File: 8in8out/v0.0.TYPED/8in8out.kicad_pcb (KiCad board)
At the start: 2 copper layers, 100.1 x 86.4 mm, 61 parts, among them IC1 ATTINY48-A, J1 RJ45, J2 RJ45, J3 CONN_6, K110 G5T-1-12VDC, K120 G5T-1-12VDC, K130 G5T-1-12VDC, K140 G5T-1-12VDC, K150 G5T-1-12VDC, K160 G5T-1-12VDC, K170 G5T-1-12VDC, K180 G5T-1-12VDC, P1 CONN_5, P100 CONN_2, P101 CONN_2, P102 CONN_2, P103 CONN_2, P105 CONN_2, P106 CONN_2, P110 CONN_2, P120 CONN_2, P130 CONN_2, P140 CONN_2, P150 CONN_2, P160 CONN_2, P170 CONN_2, P180 CONN_2, P2 CONN_5, P3 CONN_10X2, P4 CONN_2, U1 7805, U10 OPTO-TRANSISTOR, U2 ULN2803, U20 OPTO-TRANSISTOR, U30 OPTO-TRANSISTOR, U40 OPTO-TRANSISTOR, U50 OPTO-TRANSISTOR, U60 OPTO-TRANSISTOR, U70 OPTO-TRANSISTOR, U80 OPTO-TRANSISTOR

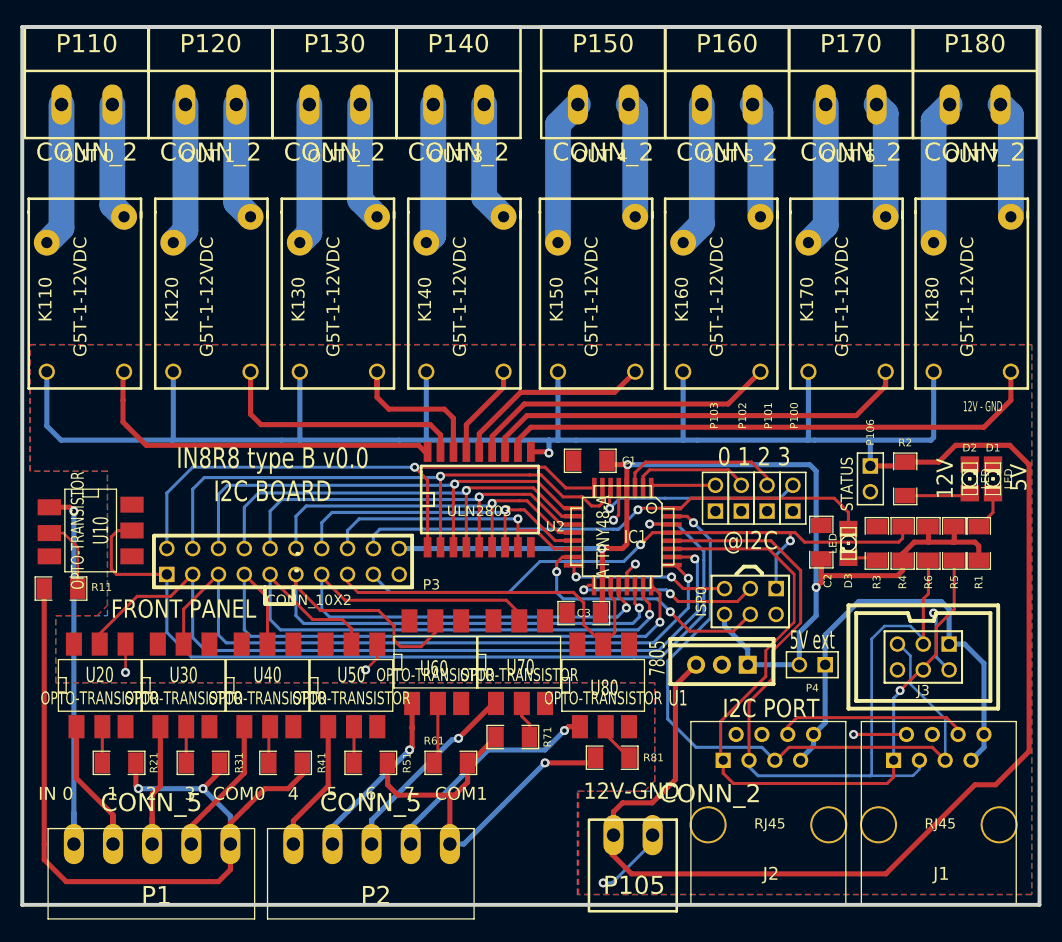
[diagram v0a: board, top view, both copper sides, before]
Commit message: correction connecteur ISP
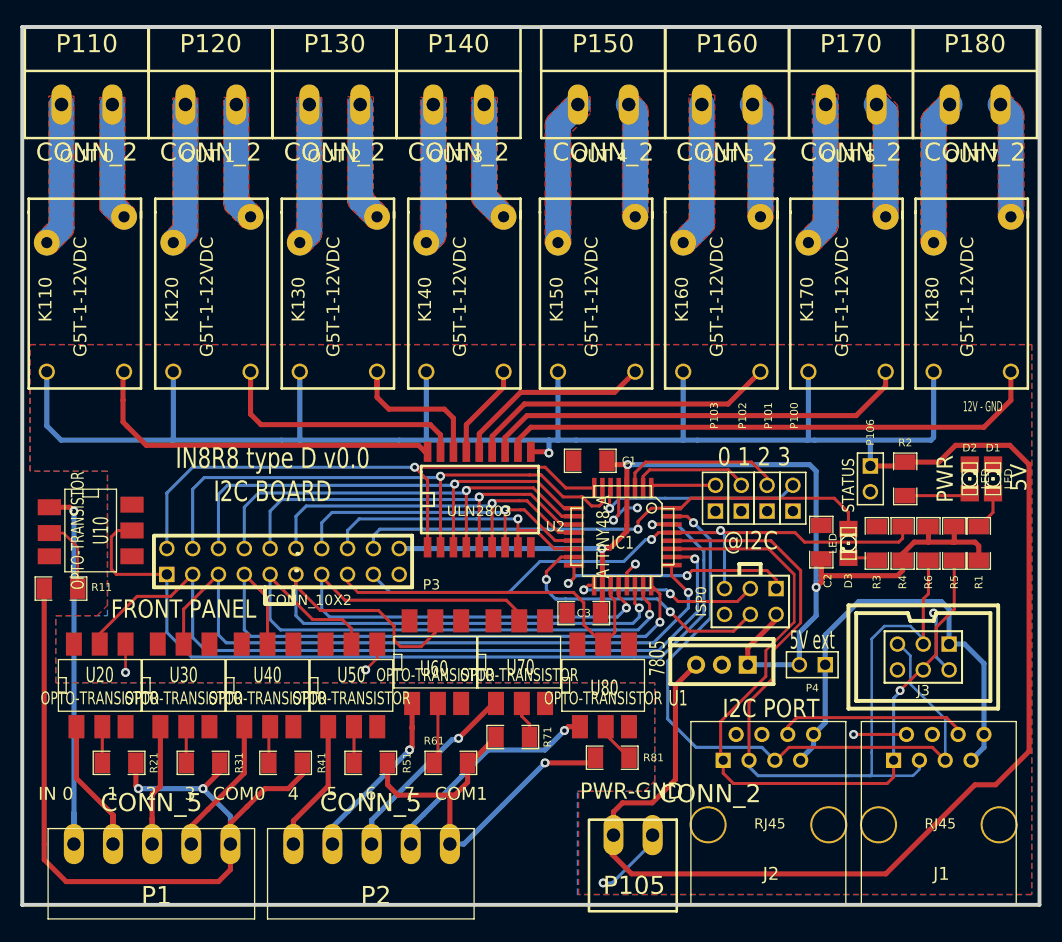
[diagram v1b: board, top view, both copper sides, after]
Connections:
- ISP0 pad 1: RESET -> MISO
- ISP0 pad 2: GND -> +5V
- ISP0 pad 5: MISO -> RESET
- ISP0 pad 6: +5V -> GND
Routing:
- net MISO: track 16.3 -> 24.4 mm
- net GND: track 50.5 -> 53.4 mm, vias 7 -> 8
- net CMD0: track 87.3 -> 89.1 mm
- net MOSI: track 26.2 -> 27.5 mm
- net +5V: track 116.1 -> 115.5 mm
- added copper zone on F.Cu, net /230_110_1
- added copper zone on F.Cu, net /230_110_2
- added copper zone on F.Cu, net /230_120_1
- added copper zone on F.Cu, net /230_120_2
- added copper zone on F.Cu, net /230_130_1
- added copper zone on F.Cu, net /230_130_2
- added copper zone on F.Cu, net /230_140_1
- added copper zone on F.Cu, net /230_140_2
- added copper zone on F.Cu, net /230_150_1
- added copper zone on F.Cu, net /230_150_2
- added copper zone on F.Cu, net /230_160_1
- added copper zone on F.Cu, net /230_160_2
- added copper zone on F.Cu, net /230_170_1
- added copper zone on F.Cu, net /230_170_2
- added copper zone on F.Cu, net /230_180_1
- added copper zone on F.Cu, net /230_180_2
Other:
- board text added: "IN8R8 type D v0.0 I2C BOARD"
- board text added: "PWR"
- board text added: "PWR-GND"
- board text removed: "12V"
- board text removed: "12V-GND"
- board text removed: "IN8R8 type B v0.0 I2C BOARD"

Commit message: reprise connecteur correction mask back connecteur 230v serigraphie complete double piste relais cot? puissance verification routage generation gerber bon pour fab ?
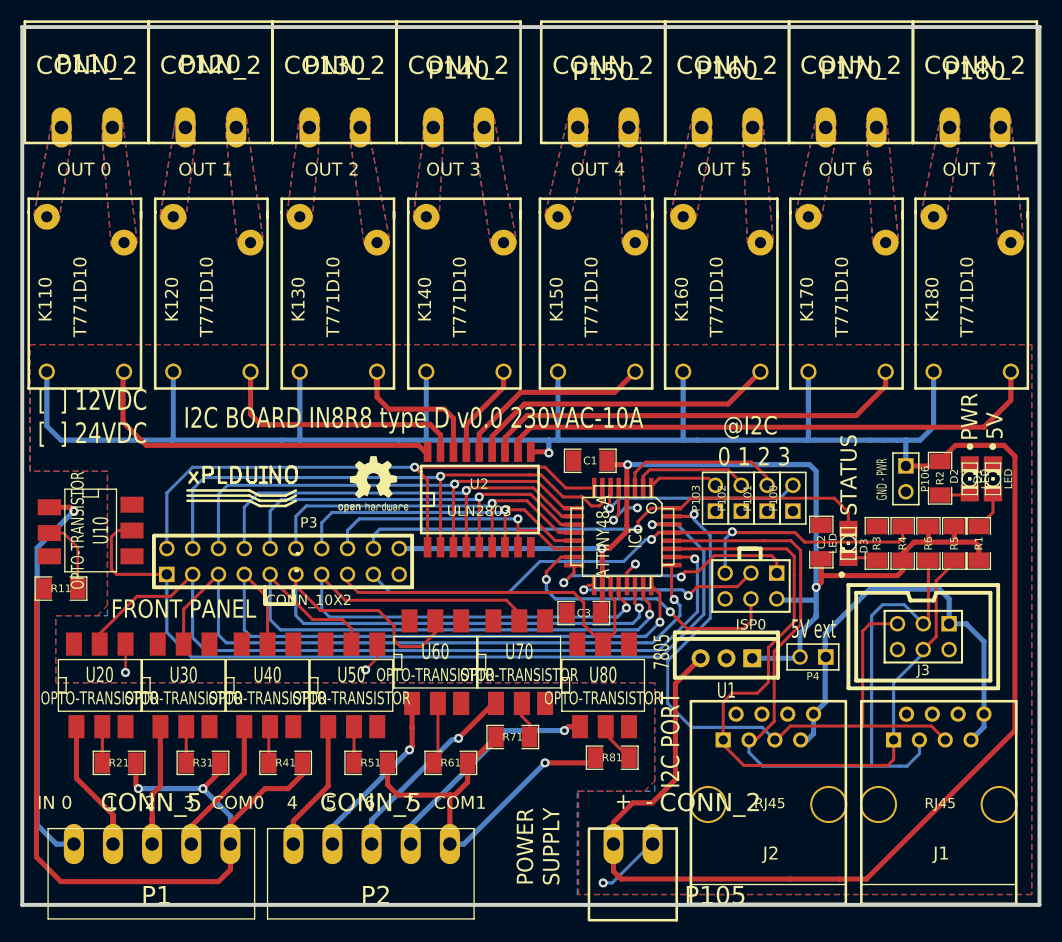
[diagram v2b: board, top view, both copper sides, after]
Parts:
- added G***: LOGO, OSHWLOGO0.3IN, F.Cu at (212.3, 112.4)
- added logo_xplduino: VAL**, logo_xplduino, F.Cu at (203.2, 117.0)
- C1, C2: value C -> 0.1uF
- C3: value C -> 4.7uF
- K110, K120, K130, K140, K150, K160, K170, K180: value G5T-1-12VDC -> T771D10
- P110, P120, P130, P140, P150, P160, P170, P180: footprint MOL_CONN_2_VH -> MOL_CONN_2_H
- moved P106 3.49 mm to (268.5, 115.6)
- moved R2 3.43 mm to (271.9, 115.5)
- moved P110 2.26 mm to (188.0, 81.0)
- moved P120 2.26 mm to (200.2, 81.0)
- moved P130 2.26 mm to (212.3, 81.0)
- moved P140 2.26 mm to (224.5, 81.0)
- moved P150 2.26 mm to (238.8, 81.0)
- moved P160 2.26 mm to (251.0, 81.0)
- moved P170 2.26 mm to (263.1, 81.0)
- moved P180 2.26 mm to (275.3, 81.0)
- moved J1 2.00 mm to (271.8, 147.6)
- moved J2 2.00 mm to (255.0, 147.6)
- moved J3 2.00 mm to (270.3, 131.1)
- moved ISP0 1.53 mm to (253.3, 126.1)
- moved P105 0.88 mm to (241.7, 151.5)
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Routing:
- net GND: track 53.4 -> 23.1 mm, vias 8 -> 6
- net /230_150_2: track 14.4 -> 0.00 mm
- net /230_160_2: track 14.3 -> 0.00 mm
- net /230_170_2: track 14.3 -> 0.00 mm
- net /230_180_2: track 14.2 -> 0.00 mm
- net /230_110_2: track 14.2 -> 0.00 mm
- net /230_120_2: track 14.1 -> 0.00 mm
- net /230_130_2: track 14.0 -> 0.00 mm
- net /230_140_2: track 13.9 -> 0.00 mm
- net /230_140_1: track 11.8 -> 0.00 mm
- net /230_130_1: track 11.7 -> 0.00 mm
- net /230_120_1: track 11.6 -> 0.00 mm
- net /230_110_1: track 11.5 -> 0.00 mm
- net /230_180_1: track 11.5 -> 0.00 mm
- net /230_170_1: track 11.4 -> 0.00 mm
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- added copper zone on B.Cu, net /230_110_1
- added copper zone on B.Cu, net /230_110_2
- added copper zone on B.Cu, net /230_120_1
- added copper zone on B.Cu, net /230_120_2
- added copper zone on B.Cu, net /230_130_1
- added copper zone on B.Cu, net /230_130_2
- added copper zone on B.Cu, net /230_140_1
- added copper zone on B.Cu, net /230_140_2
- added copper zone on B.Cu, net /230_150_1
- added copper zone on B.Cu, net /230_150_2
- added copper zone on B.Cu, net /230_160_1
- added copper zone on B.Cu, net /230_160_2
- added copper zone on B.Cu, net /230_170_1
- added copper zone on B.Cu, net /230_170_2
- added copper zone on B.Cu, net /230_180_1
- added copper zone on B.Cu, net /230_180_2
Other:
- board text added: "+ -"
- board text added: "GND - PWR"
- board text added: "I2C BOARD IN8R8 type D v0.0 230VAC-10A"
- board text added: "POWER SUPPLY"
- board text added: "[ ] 12VDC [ ] 24VDC"
- board text removed: "12V - GND"
- board text removed: "IN8R8 type D v0.0 I2C BOARD"
- board text removed: "PWR-GND"

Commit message: correction serigraphie augmentation zone isolation 12v
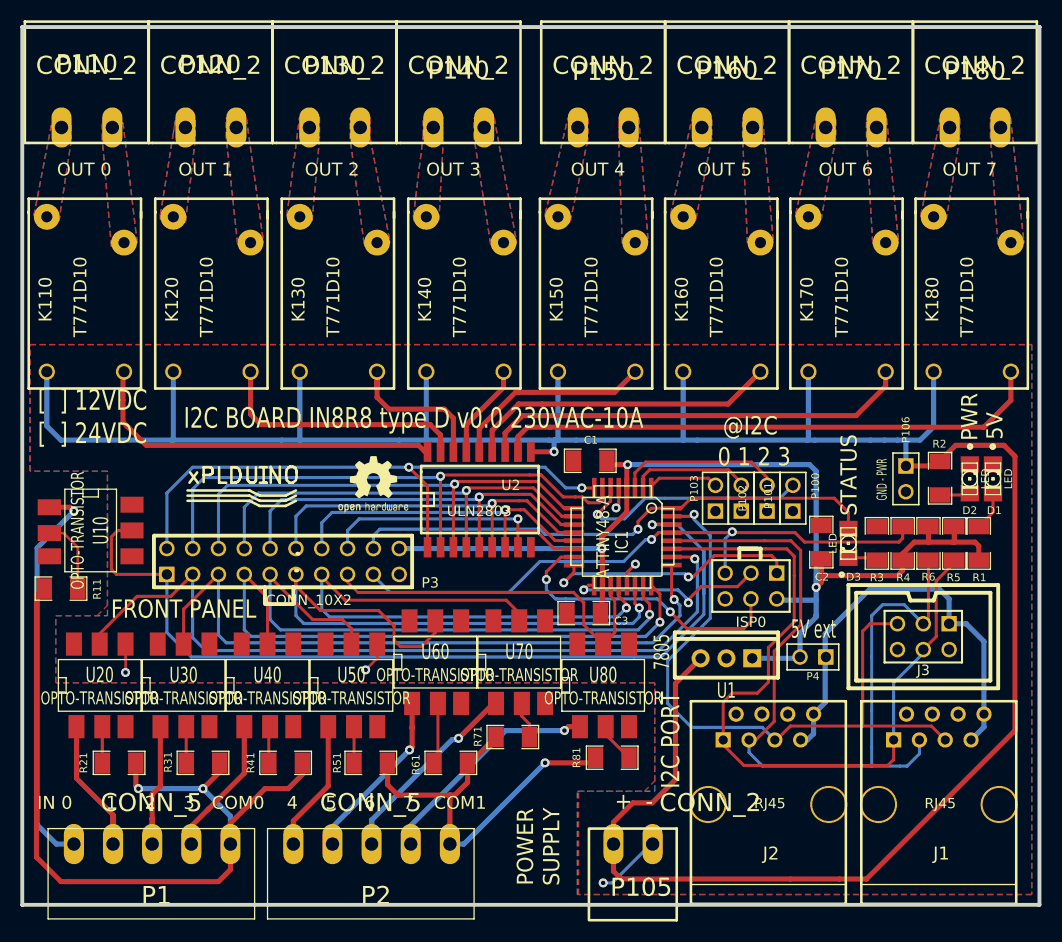
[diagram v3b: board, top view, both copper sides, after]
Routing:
- net GND: track 23.1 -> 18.9 mm, vias 6 -> 5
- net CMD0: track 89.1 -> 93.1 mm
- net A3: track 21.0 -> 23.9 mm
- net SCK: track 18.9 -> 19.8 mm
- net OUT0: track 57.8 -> 58.1 mm, vias 1 -> 2
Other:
- net class +12V: clearance 0.254 -> 0.50038

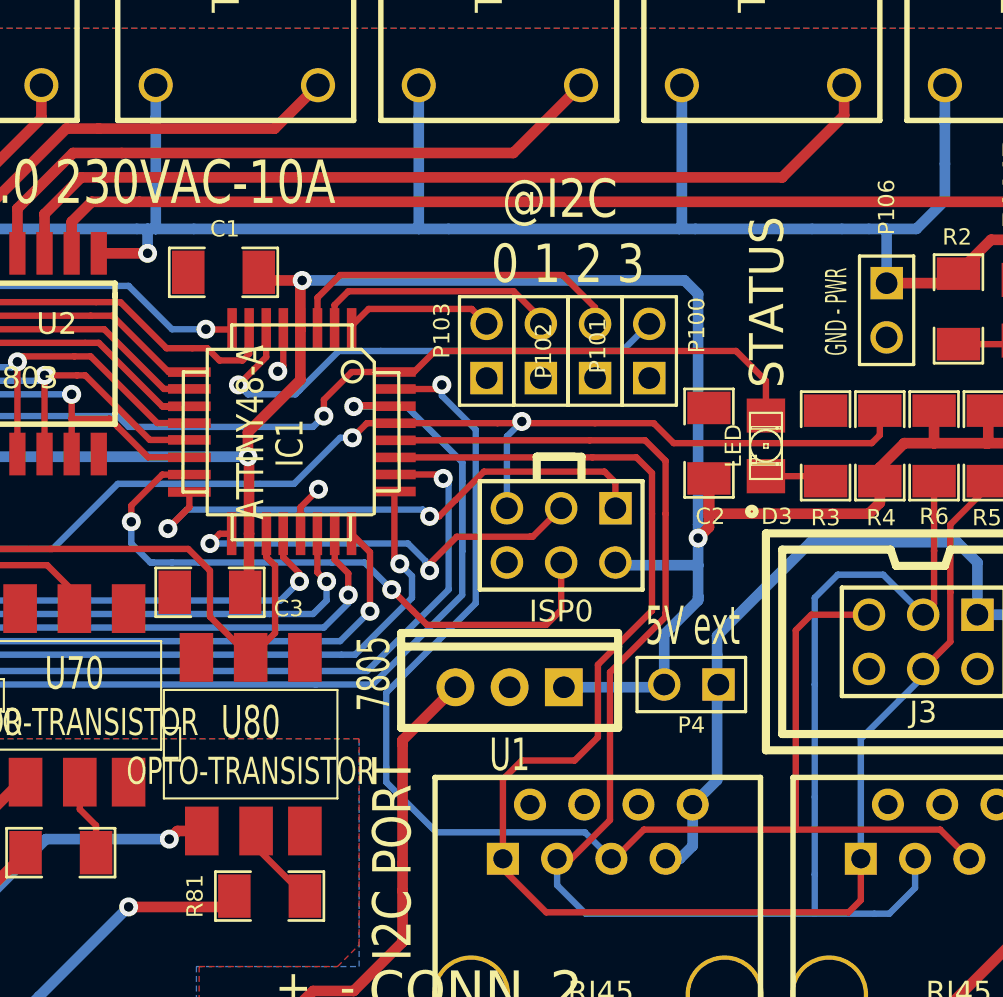
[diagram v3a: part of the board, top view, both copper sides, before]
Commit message: remplacement empreinte 7805 (TO220) par empreinte dc-dc type RECOM boug? connecteur ISP et adresse i2c pour lui laisser de la place
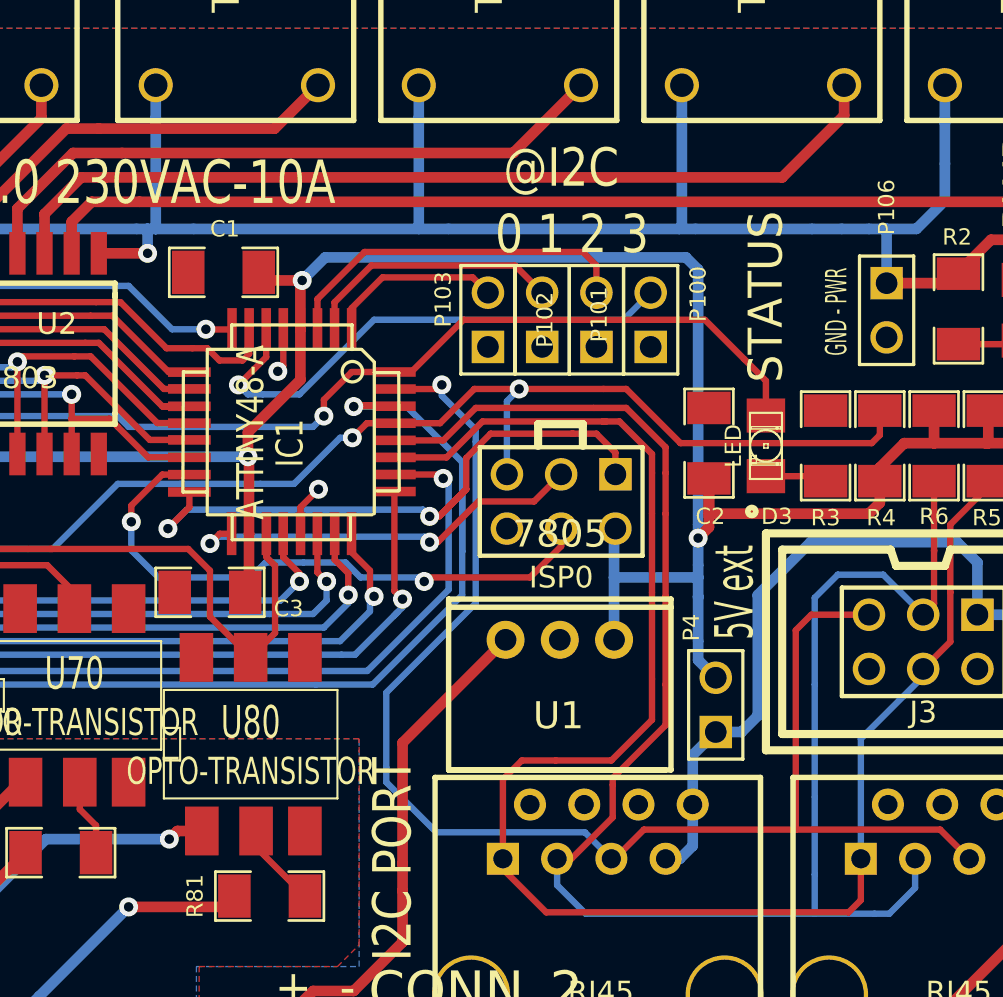
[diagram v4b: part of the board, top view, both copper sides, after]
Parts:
- U1: footprint TO220_7805_VERT -> RECOM
- moved U1 3.23 mm to (253.2, 131.0), turned to 0 degrees
- moved ISP0 1.59 mm to (253.3, 124.5)
- moved P4 1.49 mm to (260.5, 134.0), turned to 90 degrees
- moved P100 1.46 mm to (257.5, 116.0)
- moved P102 1.46 mm to (252.4, 116.0)
- moved P103 1.46 mm to (249.9, 116.0)
- moved P101 1.46 mm to (255.0, 116.0)
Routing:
- net MISO: track 25.9 -> 29.3 mm
- net +12V: track 257.4 -> 260.6 mm
- net SDA: track 75.2 -> 78.2 mm
- net +5V: track 111.8 -> 113.6 mm
- net SCL: track 82.3 -> 83.9 mm
- net LED: track 52.6 -> 53.8 mm
- net A0: track 7.11 -> 8.27 mm
- net MOSI: track 29.3 -> 28.2 mm
- net RESET: track 61.6 -> 62.6 mm
- net 5V_EXT: track 43.0 -> 43.8 mm
- net A3: track 23.9 -> 24.6 mm
- net A2: track 16.3 -> 16.9 mm
- net SCK: track 19.8 -> 19.2 mm

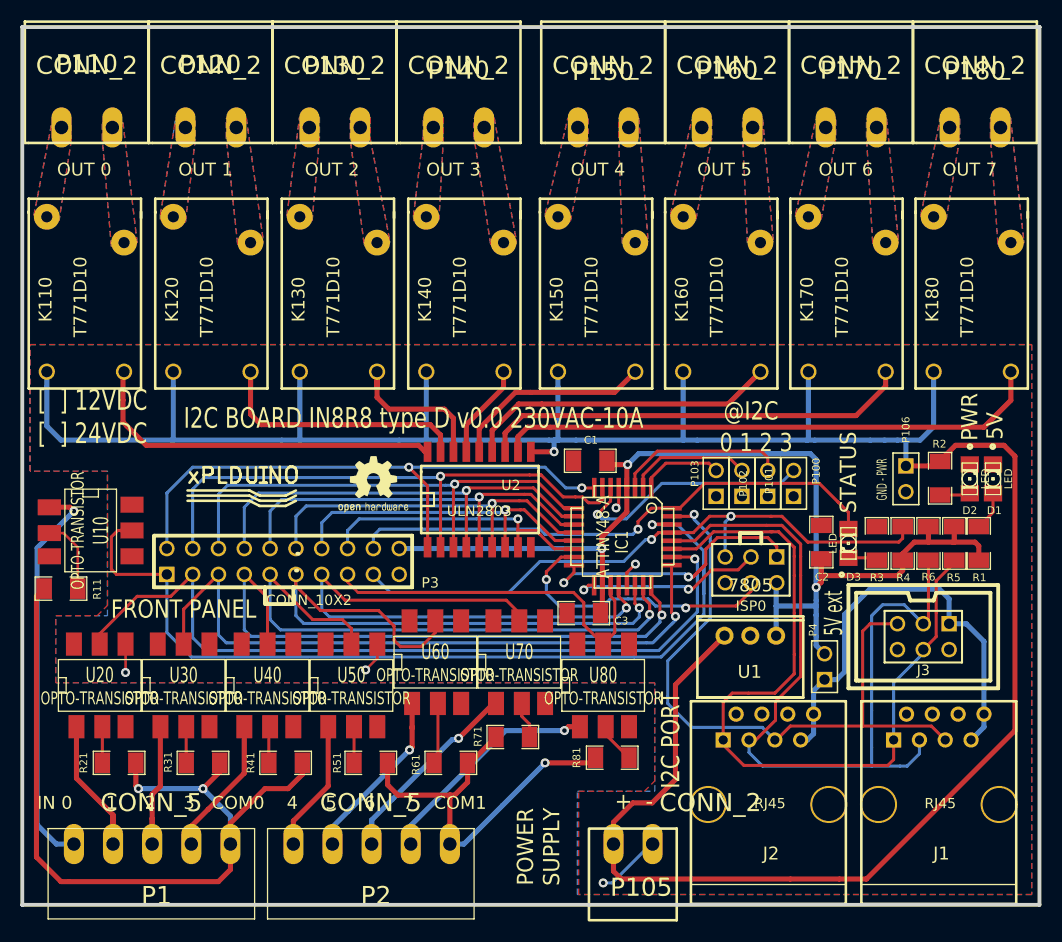
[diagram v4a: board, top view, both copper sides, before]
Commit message: ajout percage rj45 i2c (blindage) gerber pour prod
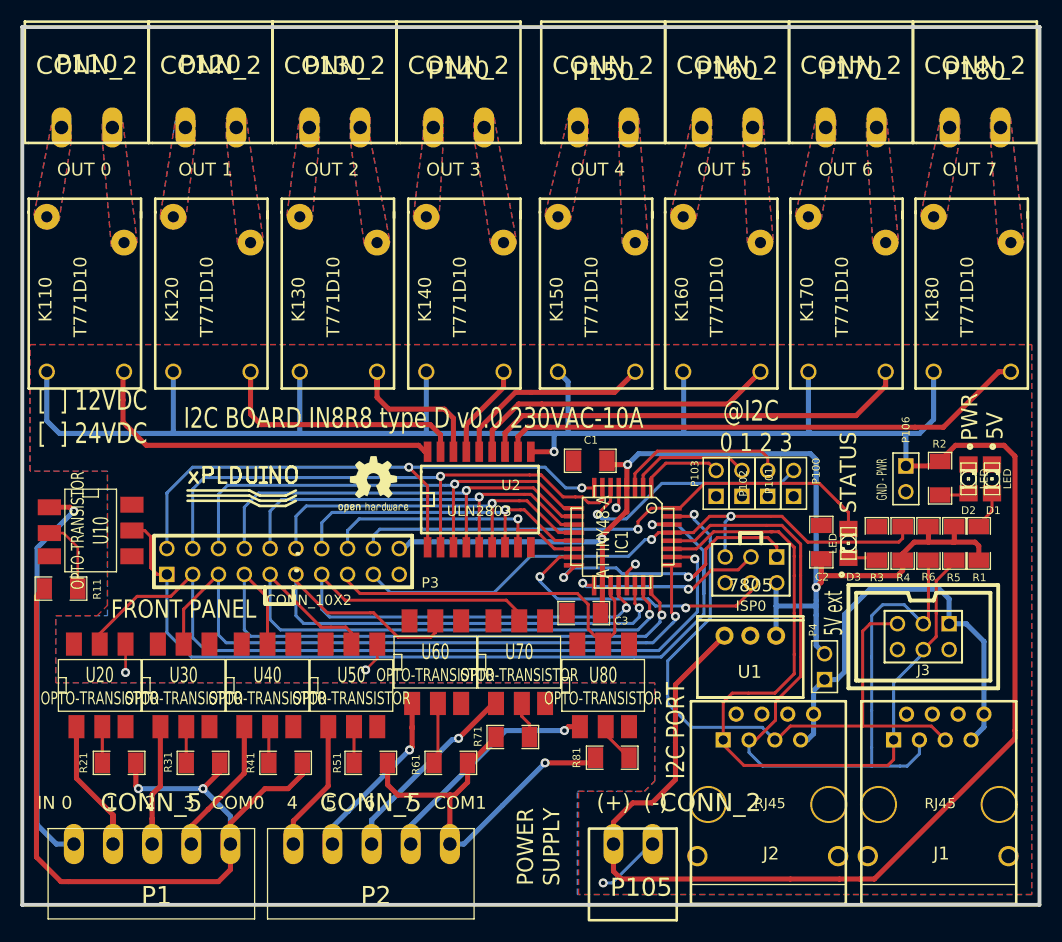
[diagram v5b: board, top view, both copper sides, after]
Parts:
- moved D2 0.13 mm to (274.7, 115.6)
- moved D1 0.10 mm to (277.0, 115.6)
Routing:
- net SCK: track 19.2 -> 29.3 mm
- net CMD0: track 93.1 -> 89.0 mm
- net +12V: track 260.6 -> 257.9 mm
- net R7: track 54.3 -> 52.6 mm
- net CMD5: track 62.5 -> 61.8 mm
- net +5V: track 113.6 -> 114.2 mm
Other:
- board text added: "(+) (-)"
- board text removed: "+ -"
